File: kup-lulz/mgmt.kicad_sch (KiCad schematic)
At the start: 3 parts, among them J13 PMOD_HOST, J14 PMOD_HOST, U9 XILINX_ULTRASCALEPLUS_B676

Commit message: Continued initial work on kup-lulz devboard
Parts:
- added C124, C125: 4.7 uF, azonenberg_pcb:EIA_0603_CAP_NOSILK, symbol device:C
- added C126, C127, C128, C129, C130, C131, C132, C133: 0.47 uF, azonenberg_pcb:EIA_0402_CAP_NOSILK, symbol device:C
- added FB3: MI0603J601R-10, azonenberg_pcb:EIA_0603_INDUCTOR_NOSILK, symbol passive-azonenberg:FERRITE_SMALL2
- added J37: XILINX_JTAG, azonenberg_pcb:XILINX_JTAG_PTH_MOLEX_0878311420, symbol xilinx-azonenberg:XILINX_JTAG
- added J38: PMOD_HOST, azonenberg_pcb:CONN_HEADER_2.54MM_2x6_RA_PMOD_HOST, symbol special-azonenberg:PMOD_HOST
- added R92: 33, azonenberg_pcb:EIA_0402_RES_NOSILK, symbol device:R
- added U14: STM32L431VxIx, azonenberg_pcb:BGA_100_7x7_DEPOP_0.5MM_STM32_UFBGA100_OSHPARK, symbol st-azonenberg:STM32L431VxIx
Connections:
- net 3V3: now also C124.1, C126.1, C128.1, C129.1, C130.1, C131.1, C132.1, C133.1, FB3.1, J37.2 (Vccaux), J38.12 (3V3), J38.6 (3V3), U14.C11 (VDD), U14.C4 (VDD), U14.E2 (VBAT), U14.G11 (VDD), U14.G12 (VDD), U14.G2 (VDD), U14.H3 (VDD)
- net GND: now also C124.2, C125.2, C126.2, C127.2, C128.2, C129.2, C130.2, C131.2, C132.2, C133.2, J37.11 (Vss), J37.3 (Vss), J37.5 (Vss), J37.7 (Vss), J37.9 (Vss), J38.11 (GND), J38.5 (GND), U14.D3 (VSS), U14.E3 (VSS), U14.F11 (VSS), U14.F12 (VSS), U14.F2 (VSS), U14.J1 (VSSA)
- new net: R92.2, U14.A8 (PB3)
- new net MCU_JTAG_TCK: J37.6 (TCK), U14.A10 (PA14)
- new net MCU_JTAG_TDI: J37.10 (TDI_OUT), U14.A9 (PA15)
- new net MCU_JTAG_TDO: J37.8 (TDO_IN), R92.1
- new net MCU_JTAG_TMS: J37.4 (TMS), U14.A11 (PA13)
- new net MCU_PMOD_DQ0: J38.1 (D0), U14.A3 (PB8)
- new net MCU_PMOD_DQ1: J38.2 (D1), U14.B3 (PB9)
- new net MCU_PMOD_DQ2: J38.3 (D2), U14.L10 (PB10)
- new net MCU_PMOD_DQ3: J38.4 (D3), U14.L11 (PB11)
- new net MCU_PMOD_DQ4: J38.7 (D4), U14.L12 (PB12)
- new net MCU_PMOD_DQ5: J38.8 (D5), U14.K12 (PB13)
- new net MCU_PMOD_DQ6: J38.9 (D6), U14.K11 (PB14)
- new net MCU_PMOD_DQ7: J38.10 (D7), U14.K10 (PB15)
- new net MCU_VDDA: C125.1, C127.1, FB3.2, U14.M1 (VDDA)
- no-connect marks 8 -> 10
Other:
- note added: "MCU VDDA decoupling"

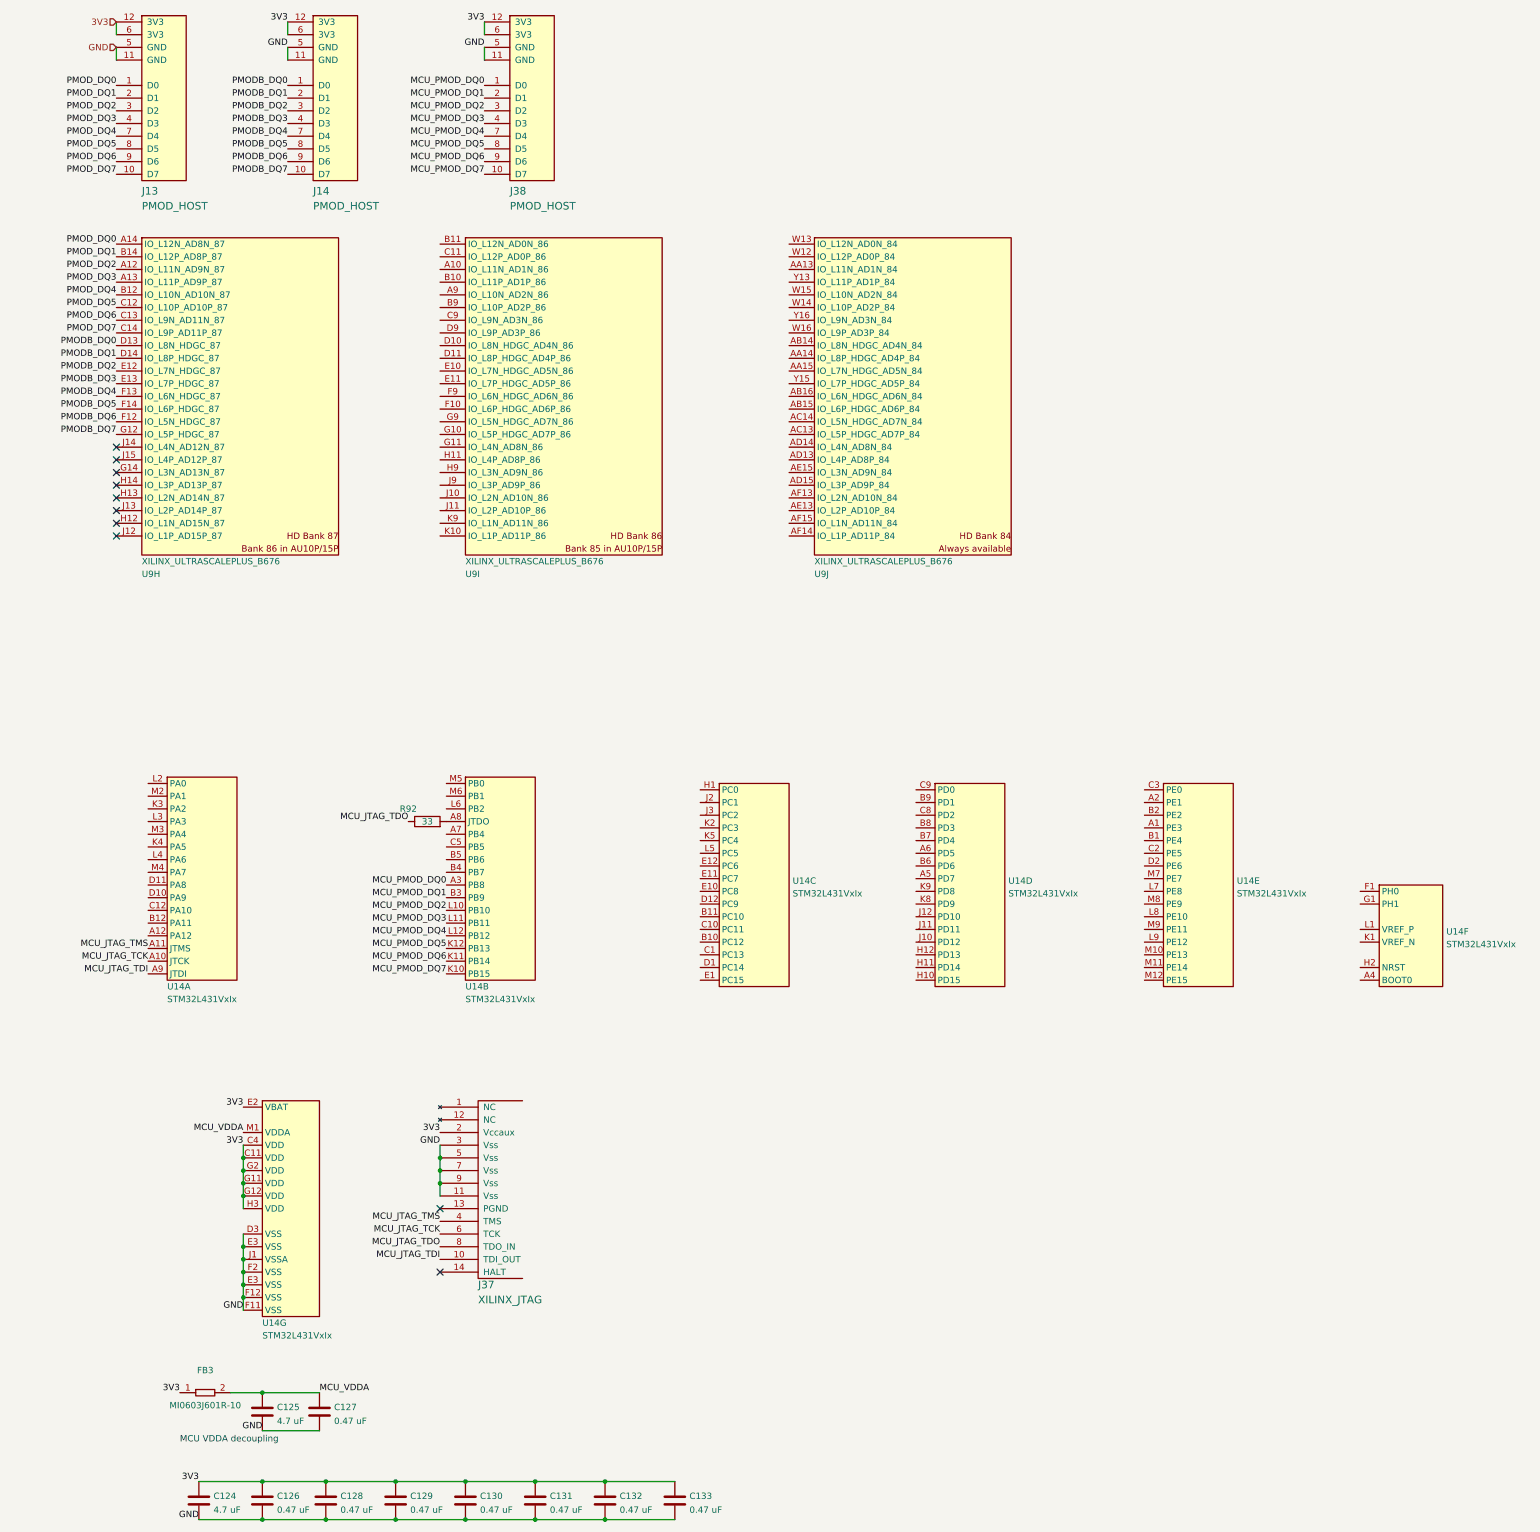
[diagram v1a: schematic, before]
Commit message: Continued initial layout of kup-lulz
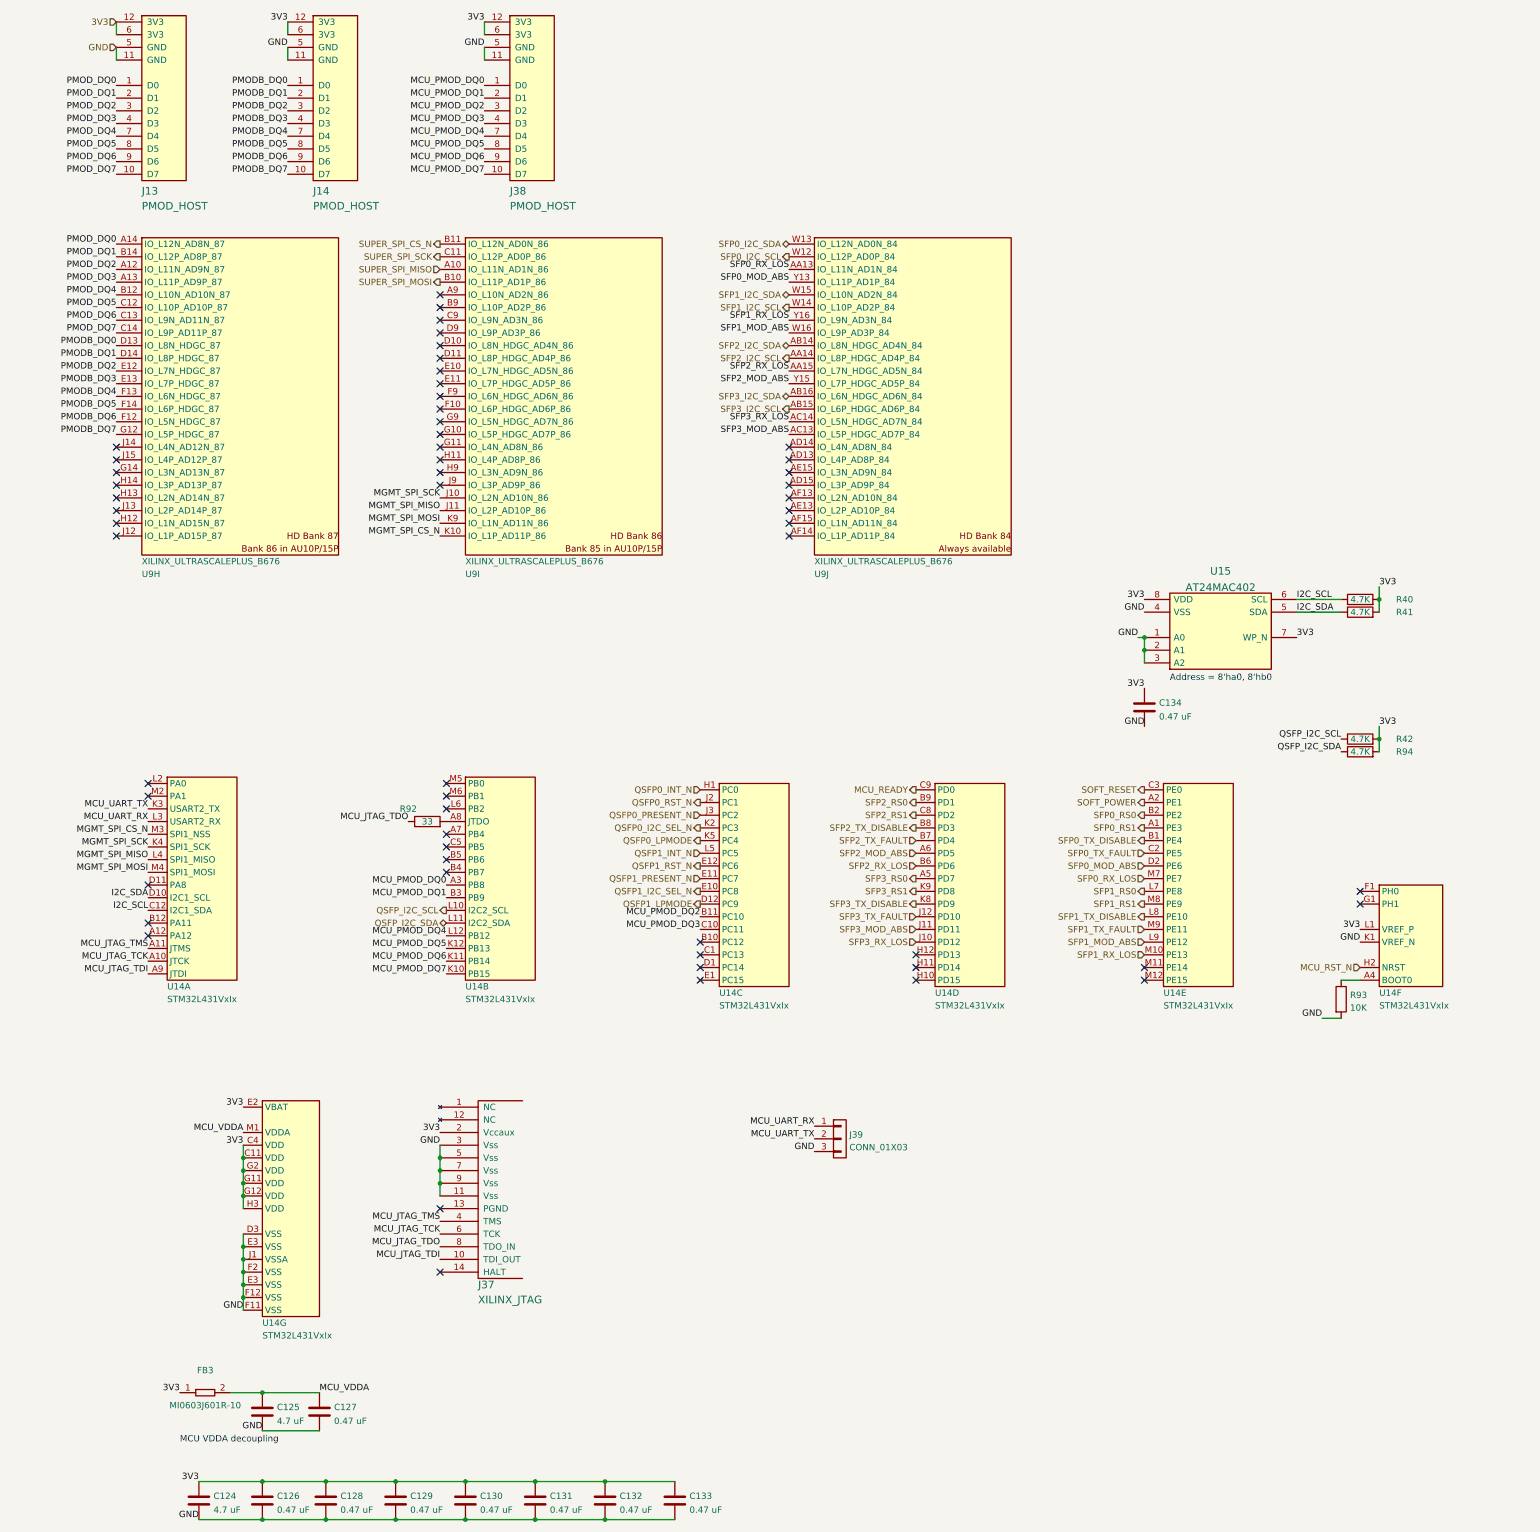
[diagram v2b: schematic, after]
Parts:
- added C134: 0.47 uF, azonenberg_pcb:EIA_0402_CAP_NOSILK, symbol device:C
- added J39: CONN_01X03, azonenberg_pcb:CONN_HEADER_2.54MM_1x3, symbol conn:CONN_01X03
- added R40, R41, R42, R94: 4.7K, azonenberg_pcb:EIA_0402_RES_NOSILK, symbol device:R
- added R93: 10K, azonenberg_pcb:EIA_0402_RES_NOSILK, symbol device:R
- added U15: AT24MAC402, azonenberg_pcb:DFN_8_0.5MM_2x3MM_TALL, symbol memory-azonenberg:24Cxx-DFN8
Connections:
- net 3V3: now also U14.L1 (VREF_P), C134.1, R40.2, R41.2, R42.2, R94.2, U15.7 (WP_N), U15.8 (VDD)
- net GND: now also U14.K1 (VREF_N), C134.2, J39.3 (P3), R93.2, U15.1 (A0), U15.2 (A1), U15.3 (A2), U15.4 (VSS)
- net MCU_PMOD_DQ2: now also U14.B11 (PC10); no longer U14.L10 (PB10)
- net MCU_PMOD_DQ3: now also U14.C10 (PC11); no longer U14.L11 (PB11)
- net SUPER_SPI_MISO: now reaches U9.A10 (IO_L11N_AD1N_86)
- net SUPER_SPI_MOSI: now reaches U9.B10 (IO_L11P_AD1P_86)
- net SUPER_SPI_CS_N: now reaches U9.B11 (IO_L12N_AD0N_86)
- net SUPER_SPI_SCK: now reaches U9.C11 (IO_L12P_AD0P_86)
- net MGMT_SPI_SCK: now reaches U9.J10 (IO_L2N_AD10N_86)
- net MGMT_SPI_SCK: now also U14.K4 (PA5)
- net MGMT_SPI_MISO: now reaches U9.J11 (IO_L2P_AD10P_86)
- net MGMT_SPI_MISO: now also U14.L4 (PA6)
- net MGMT_SPI_CS_N: now reaches U9.K10 (IO_L1P_AD11P_86)
- net MGMT_SPI_CS_N: now also U14.M3 (PA4)
- net MGMT_SPI_MOSI: now reaches U9.K9 (IO_L1N_AD11N_86)
- net MGMT_SPI_MOSI: now also U14.M4 (PA7)
- net SFP0_RX_LOS: now reaches U9.AA13 (IO_L11N_AD1N_84)
- net SFP0_RX_LOS: now also U14.M7 (PE7)
- net SFP2_I2C_SCL: now reaches U9.AA14 (IO_L8P_HDGC_AD4P_84)
- net SFP2_RX_LOS: now reaches U9.AA15 (IO_L7N_HDGC_AD5N_84)
- net SFP2_RX_LOS: now also U14.B6 (PD6)
- net SFP2_I2C_SDA: now reaches U9.AB14 (IO_L8N_HDGC_AD4N_84)
- net SFP3_I2C_SCL: now reaches U9.AB15 (IO_L6P_HDGC_AD6P_84)
- net SFP3_I2C_SDA: now reaches U9.AB16 (IO_L6N_HDGC_AD6N_84)
- net SFP3_MOD_ABS: now reaches U9.AC13 (IO_L5P_HDGC_AD7P_84)
- net SFP3_MOD_ABS: now also U14.J11 (PD11)
- net SFP3_RX_LOS: now reaches U9.AC14 (IO_L5N_HDGC_AD7N_84)
- net SFP3_RX_LOS: now also U14.J10 (PD12)
- net SFP0_I2C_SCL: now reaches U9.W12 (IO_L12P_AD0P_84)
- net SFP0_I2C_SDA: now reaches U9.W13 (IO_L12N_AD0N_84)
- net SFP1_I2C_SCL: now reaches U9.W14 (IO_L10P_AD2P_84)
- net SFP1_I2C_SDA: now reaches U9.W15 (IO_L10N_AD2N_84)
- net SFP1_MOD_ABS: now reaches U9.W16 (IO_L9P_AD3P_84)
- net SFP1_MOD_ABS: now also U14.L9 (PE12)
- net SFP0_MOD_ABS: now reaches U9.Y13 (IO_L11P_AD1P_84)
- net SFP0_MOD_ABS: now also U14.D2 (PE6)
- net SFP2_MOD_ABS: now reaches U9.Y15 (IO_L7P_HDGC_AD5P_84)
- net SFP2_MOD_ABS: now also U14.A6 (PD5)
- net SFP1_RX_LOS: now reaches U9.Y16 (IO_L9N_AD3N_84)
- net SFP1_RX_LOS: now also U14.M10 (PE13)
- net I2C_SCL: now reaches U14.C12 (PA10)
- net I2C_SCL: now also R40.1, U15.6 (SCL)
- net I2C_SDA: now reaches U14.D10 (PA9)
- net I2C_SDA: now also R41.1, U15.5 (SDA)
- net MCU_UART_TX: now reaches U14.K3 (PA2)
- net MCU_UART_TX: now also J39.2 (P2)
- net MCU_UART_RX: now reaches U14.L3 (PA3)
- net MCU_UART_RX: now also J39.1 (P1)
- net at U14.A4 (BOOT0): now also R93.1
- net MCU_RST_N: now reaches U14.H2 (NRST)
- net SFP0_RS1: now reaches U14.A1 (PE3)
- net SOFT_POWER: now reaches U14.A2 (PE1)
- net SFP0_TX_DISABLE: now reaches U14.B1 (PE4)
- net SFP0_RS0: now reaches U14.B2 (PE2)
- net SFP0_TX_FAULT: now reaches U14.C2 (PE5)
- net SOFT_RESET: now reaches U14.C3 (PE0)
- net SFP1_RS0: now reaches U14.L7 (PE8)
- net SFP1_TX_DISABLE: now reaches U14.L8 (PE10)
- net SFP1_RS1: now reaches U14.M8 (PE9)
- net SFP1_TX_FAULT: now reaches U14.M9 (PE11)
- net QSFP1_LPMODE: now reaches U14.D12 (PC9)
- net QSFP1_I2C_SEL_N: now reaches U14.E10 (PC8)
- net QSFP1_PRESENT_N: now reaches U14.E11 (PC7)
- net QSFP1_RST_N: now reaches U14.E12 (PC6)
- net QSFP0_INT_N: now reaches U14.H1 (PC0)
- net QSFP0_RST_N: now reaches U14.J2 (PC1)
- net QSFP0_PRESENT_N: now reaches U14.J3 (PC2)
- net QSFP0_I2C_SEL_N: now reaches U14.K2 (PC3)
- net QSFP0_LPMODE: now reaches U14.K5 (PC4)
- net QSFP1_INT_N: now reaches U14.L5 (PC5)
- net SFP3_RS0: now reaches U14.A5 (PD7)
- net SFP2_TX_FAULT: now reaches U14.B7 (PD4)
- net SFP2_TX_DISABLE: now reaches U14.B8 (PD3)
- net SFP2_RS0: now reaches U14.B9 (PD1)
- net SFP2_RS1: now reaches U14.C8 (PD2)
- net MCU_READY: now reaches U14.C9 (PD0)
- net SFP3_TX_FAULT: now reaches U14.J12 (PD10)
- net SFP3_TX_DISABLE: now reaches U14.K8 (PD9)
- net SFP3_RS1: now reaches U14.K9 (PD8)
- new net QSFP_I2C_SCL: R42.1, U14.L10 (PB10)
- new net QSFP_I2C_SDA: R94.1, U14.L11 (PB11)
- no-connect marks 10 -> 57
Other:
- note added: "Address = 8'ha0, 8'hb0"
- company: (none) -> Antikernel Labs
